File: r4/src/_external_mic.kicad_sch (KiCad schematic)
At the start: 132 parts, among them Q12 BSS84PW, Q13 BSS84PW, Q14 NX6008NBKW, Q15 NX3008NBKW, Q16 NX3008NBKW, Q17 NX3008NBKW, Q18 NX3008NBKW, Q19 NX3008NBKW, Q20 BSS84PW, Q21 BSS84PW, Q22 NX3008NBKW, Q23 NX3008NBKW, Q24 NX3008NBKW, Q25 BSS84PW, T18 , T19 , T20 , T23 , T24 , T25 , T26 , T27 , T28 , T29 , T30 , T31 , T32 , T33 , T34 , T35 , T37 , T38 , T43 , T44 , T45 , T46 , T47 , T48 , T49 , T50 , U17 74HC20, U18 THAT5173, U19 74HC74, U20 74HC132, U21 74HC4520, U22 74HC132, U23 THAT1580, U24 74HC688, U25 LM4562, U26 74HC688, U27 AD4005

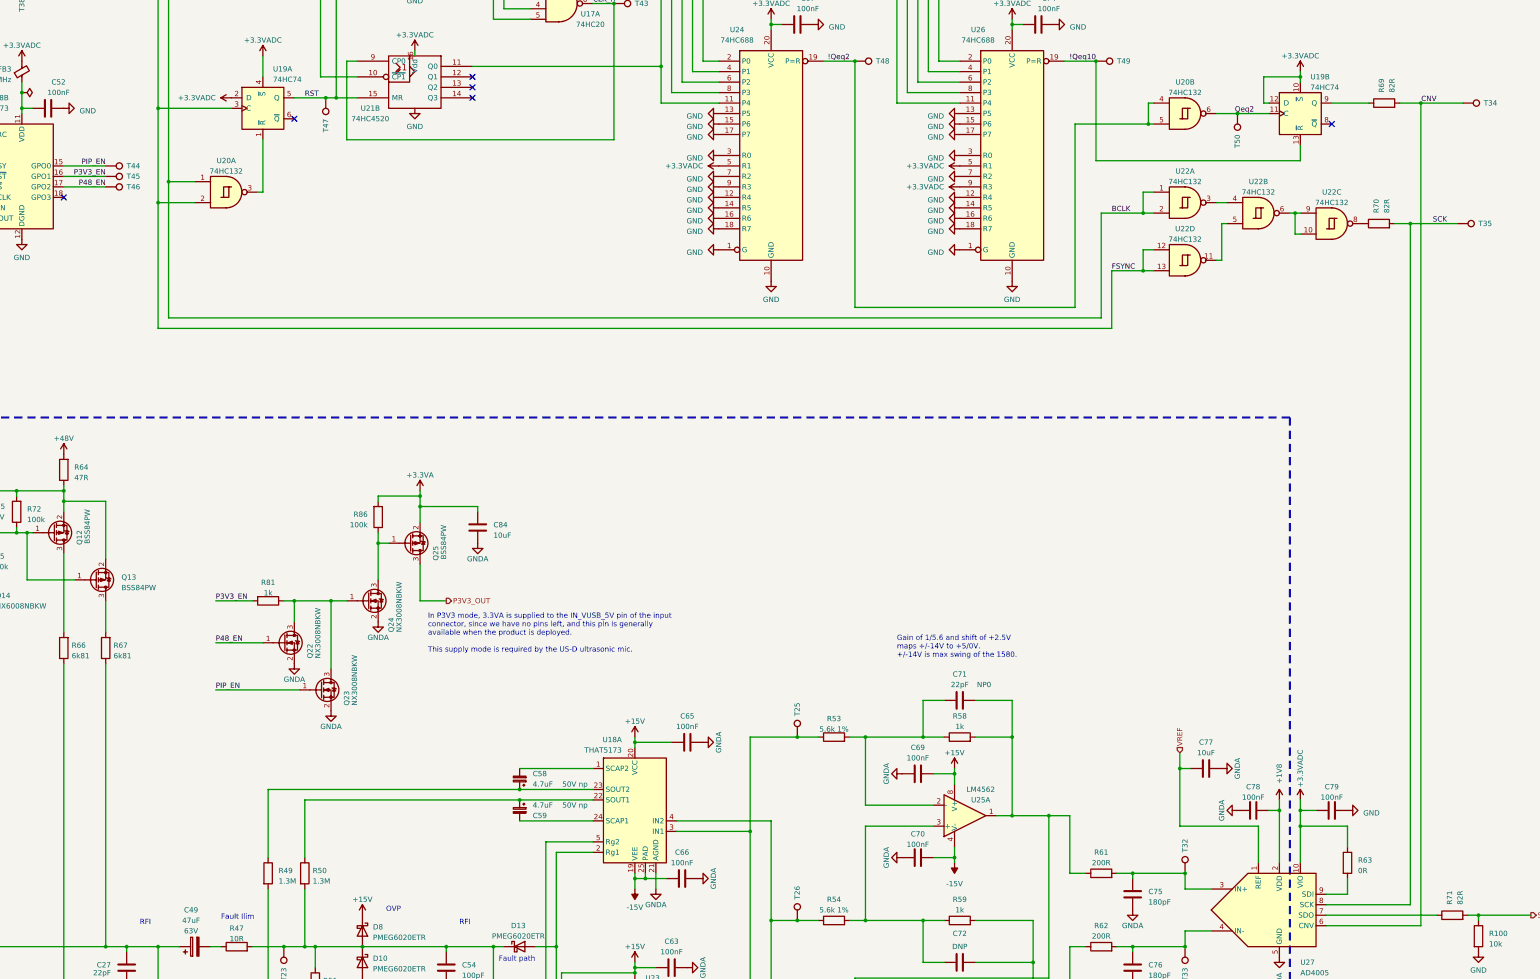
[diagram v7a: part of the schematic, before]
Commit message: Change some passive values and packages to get rid of some BOM lines
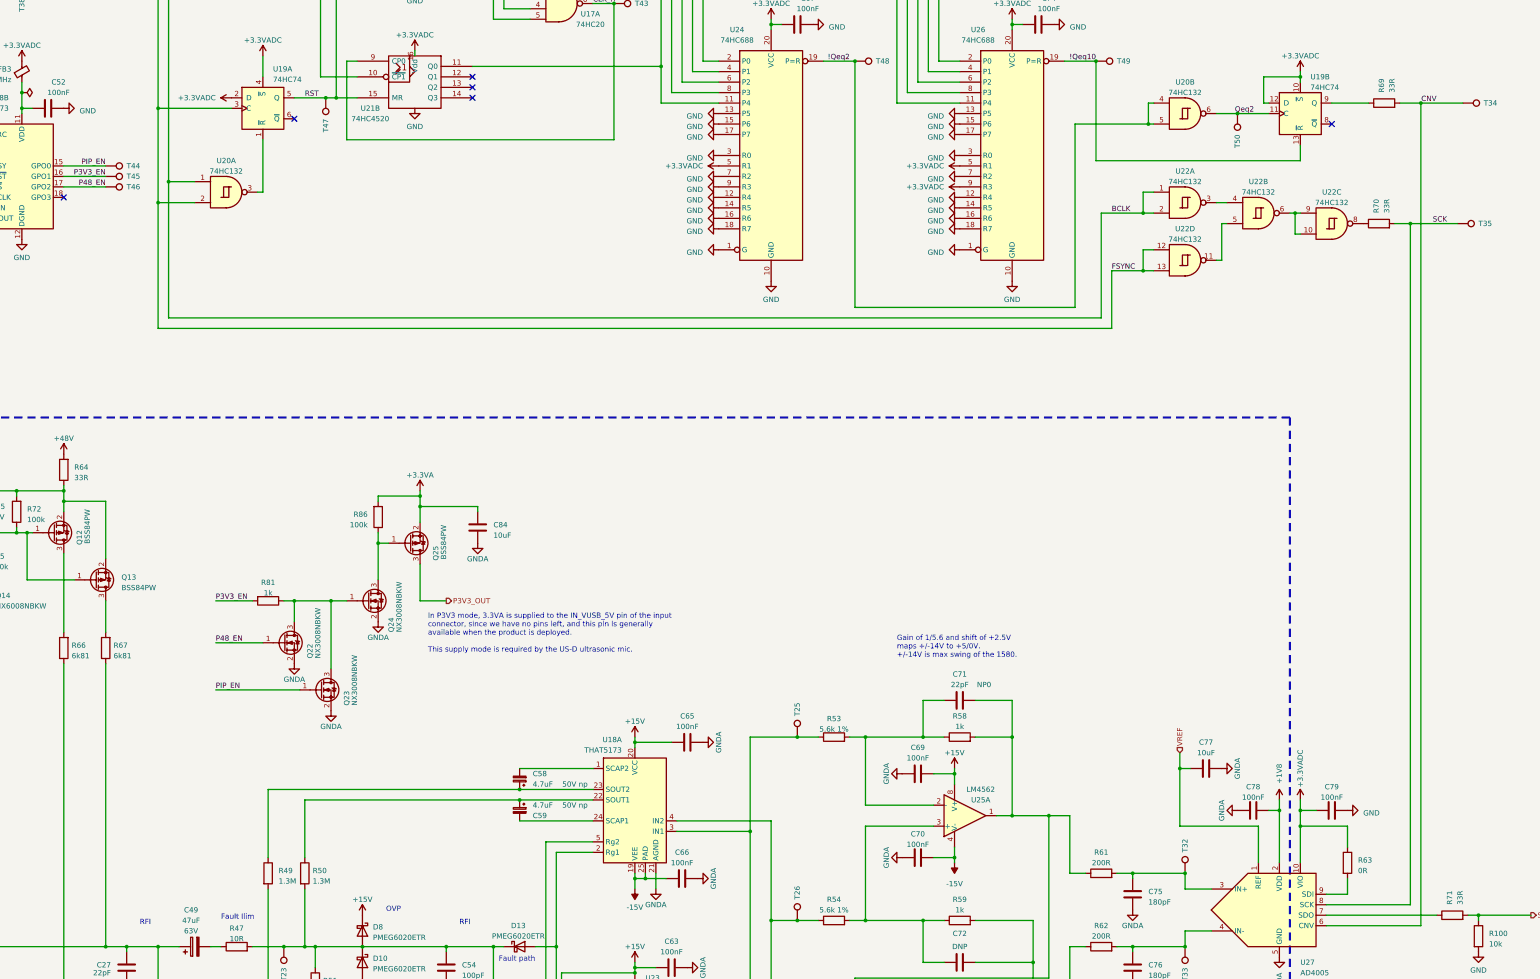
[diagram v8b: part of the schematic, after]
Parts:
- R64: value 47R -> 33R
- R69, R70, R71: value 82R -> 33R
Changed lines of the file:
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@@
       (effects (font (size 1.27 1.27)) (justify left))
     )
-    (property "Value" "82R" (at 540.385 308.61 0)
+    (property "Value" "33R" (at 540.385 308.61 0)
       (effects (font (size 1.27 1.27)) (justify left))
     )
@@
       (project "bugg-main-r4"
         (path "/e3eb514f-6ce4-4abe-ba20-f82f0015628f/41f15edd-4583-4f5d-8a81-daeb7c83b416"
-          (reference "R71") (unit 1) (value "82R") (footprint "Resistor_SMD:R_0402_1005Metric")
+          (reference "R71") (unit 1) (value "33R") (footprint "Resistor_SMD:R_0402_1005Metric")
         )
       )
@@
       (effects (font (size 1.27 1.27)) (justify left))
     )
-    (property "Value" "82R" (at 522.605 140.97 0)
+    (property "Value" "33R" (at 522.605 140.97 0)
       (effects (font (size 1.27 1.27)) (justify left))
     )
@@
       (project "bugg-main-r4"
         (path "/e3eb514f-6ce4-4abe-ba20-f82f0015628f/41f15edd-4583-4f5d-8a81-daeb7c83b416"
-          (reference "R70") (unit 1) (value "82R") (footprint "Resistor_SMD:R_0402_1005Metric")
+          (reference "R70") (unit 1) (value "33R") (footprint "Resistor_SMD:R_0402_1005Metric")
         )
       )
@@
       (effects (font (size 1.27 1.27)) (justify left))
     )
-    (property "Value" "82R" (at 523.875 111.76 0)
+    (property "Value" "33R" (at 523.875 111.76 0)
       (effects (font (size 1.27 1.27)) (justify left))
     )
@@
       (project "bugg-main-r4"
         (path "/e3eb514f-6ce4-4abe-ba20-f82f0015628f/41f15edd-4583-4f5d-8a81-daeb7c83b416"
-          (reference "R69") (unit 1) (value "82R") (footprint "Resistor_SMD:R_0402_1005Metric")
+          (reference "R69") (unit 1) (value "33R") (footprint "Resistor_SMD:R_0402_1005Metric")
         )
       )
@@
       (effects (font (size 1.27 1.27)) (justify right))
     )
-    (property "Value" "47R" (at 204.47 205.105 0)
+    (property "Value" "33R" (at 204.47 205.105 0)
       (effects (font (size 1.27 1.27)) (justify right))
     )
@@
       (project "bugg-main-r4"
         (path "/e3eb514f-6ce4-4abe-ba20-f82f0015628f/41f15edd-4583-4f5d-8a81-daeb7c83b416"
-          (reference "R64") (unit 1) (value "47R") (footprint "Resistor_SMD:R_0402_1005Metric")
-        )
-      )
+          (reference "R64") (unit 1) (value "33R") (footprint "Resistor_SMD:R_0402_1005Metric")
+        )
+      )
